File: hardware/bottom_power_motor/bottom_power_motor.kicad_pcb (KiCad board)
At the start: 2 copper layers, 52 x 52 mm, 104 parts, among them J1 Power/Motor 6p, J2 J_STK_A, J3 J_STK_B, Q1 P-FET 40V 30A, U1 L78L12, U2 TPS54360, U2_CB 100n, U2_CO 47u, U2_CZ 3n3, U2_D 60V 3A, U2_L 10u, U2_RC 10k, U2_RH 53k6, U2_RL 10k2, U2_RT_R 100k, U3 TLV62569, U4 TPS54360, U4_CB 100n, U4_CO 22u, U4_CZ 3n3, U4_D 60V 3A, U4_L 33u, U4_RC 10k, U4_RH 68k1, U4_RL 10k0, U4_RT_R 100k

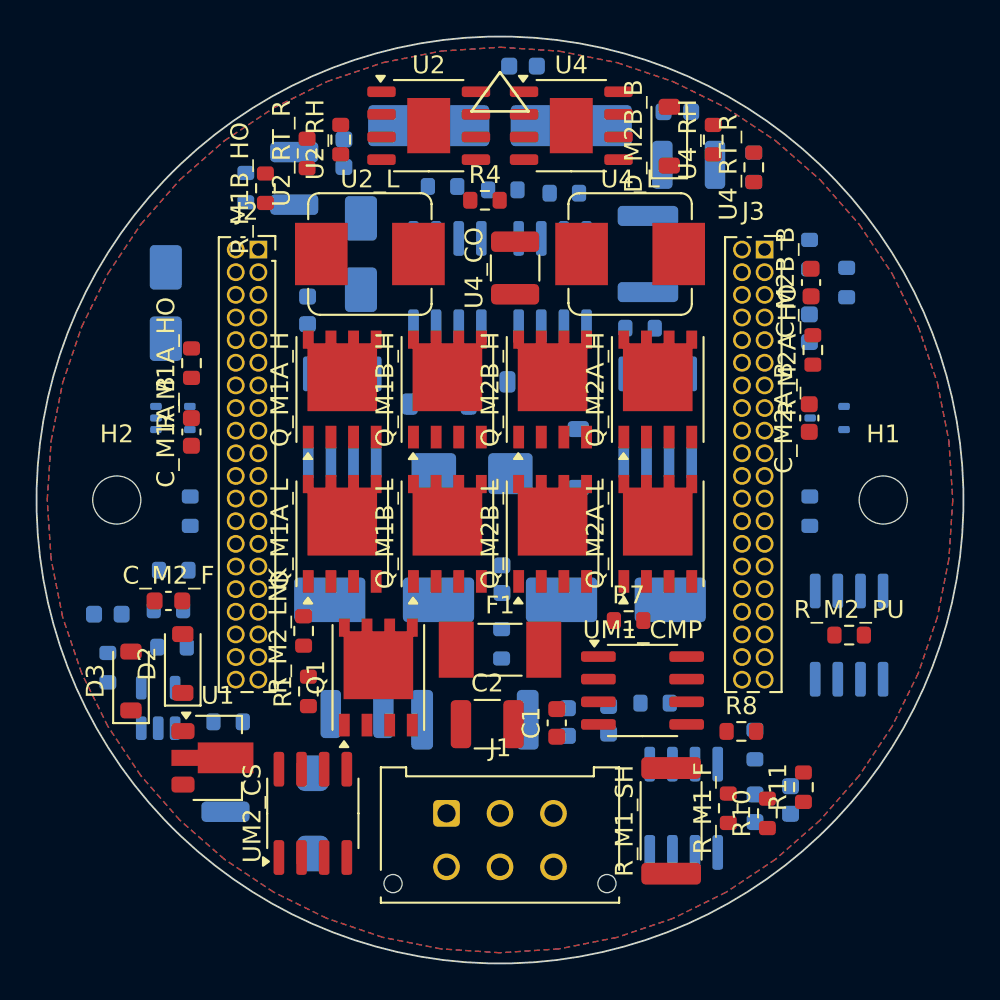
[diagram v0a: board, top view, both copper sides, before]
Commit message: Zwischenstand: Bottom neu geroutet, Top-Masse in Arbeit
Bottom: Neurouting mit 0,8-mm-Klasse - keine Kupferfehler mehr, aber
noch 62 offene Verbindungen; ein Fortsetzungslauf (Export mit
bestehender Verdrahtung, type route) konvergiert gerade weiter.
Top: Masse-Stichbahnen importiert und Zonen neu gefuellt (offene
PGND-Paare von 17 auf 7 reduziert); USB-Schirmpads A1/A12 per Stub an
die B-Reihe angebunden. Die restlichen 7 sitzen hinter USB-Datenbahnen
- USB_DP_C/DN_C, QSPI_D0 und RADAR_INT sind dafuer aufgerissen und
werden zusammen mit PGND als Netz neu verlegt (laeuft im Hintergrund).
route_boards: SWIG-Zaehlfehler nach SaveBoard umgangen (Zahlen kommen
aus dem eigenen SES-Import).

Co-Authored-By: Claude Fable 5 <noreply@anthropic.com>
Claude-Session: https://claude.ai/code/session_017FTFDJW9R41k2WFeDRNE3w
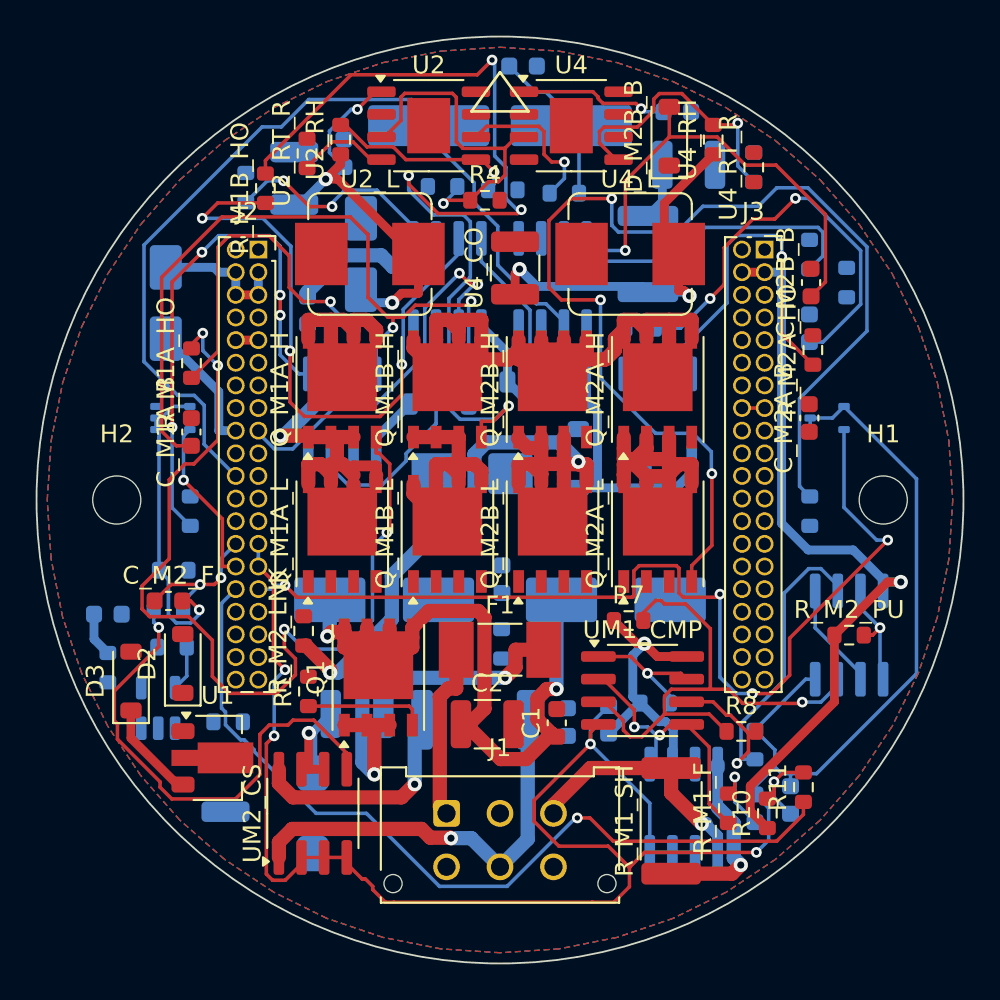
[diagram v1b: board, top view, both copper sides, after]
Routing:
- net AGND: track 0.00 -> 138.2 mm, vias 0 -> 5
- net 24V_PROT: track 0.00 -> 88.1 mm, vias 0 -> 2
- net 3V3_SYS: track 0.00 -> 68.5 mm, vias 0 -> 3
- net M2A_LO_GT: track 0.00 -> 65.2 mm, vias 0 -> 3
- net HW_TRIP2: track 0.00 -> 56.2 mm, vias 0 -> 4
- net M1B_HO_GT: track 0.00 -> 55.2 mm, vias 0 -> 4
- net M1A_HO_GT: track 0.00 -> 51.2 mm, vias 0 -> 4
- net M2_INB: track 0.00 -> 50.6 mm
- net TRIP_RST: track 0.00 -> 47.7 mm, vias 0 -> 1
- net M1A_VB: track 0.00 -> 43.6 mm, vias 0 -> 2
- net M2_SWB: track 0.00 -> 40.3 mm, vias 0 -> 2
- net M1B_HO_G: track 0.00 -> 35.5 mm, vias 0 -> 3
- net M2_ISNS: track 0.00 -> 33.7 mm, vias 0 -> 1
- net M1_SWA: track 0.00 -> 31.7 mm, vias 0 -> 2
- net M2_SWA: track 0.00 -> 30.1 mm, vias 0 -> 1
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
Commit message: Bottom: Standard-Vias und -Clearance fuer Leistungsklassen
Die 0,8er-Vias mit 0,2er-Clearance passen nicht in die Schluchten
zwischen den FET-Pads - die letzten ~50 Verbindungen blieben ueber
mehrere Stunden Autorouting dauerhaft offen. Jetzt 0,6/0,3-Vias und
0,15er-Clearance auch fuer PWR/RAIL auf dem Bottom-Board (2-3 A je
Via, ausreichend fuer Laufstrom und kurze Transienten; Handnacharbeit
der Leistungspfade vor Fertigung bleibt Pflicht per docs/05).
Bottom-Fortsetzungslauf mit den entspannten Regeln laeuft. Zudem
Bottom-Stand nach erster Fortsetzung (62 -> 53 offen) und Mid-Stand
nach finalem Wandnetz-Lauf (J3-25/33-Kette per Stich angebunden,
7 Paare offen, Iterator laeuft) uebernommen.

Co-Authored-By: Claude Fable 5 <noreply@anthropic.com>
Claude-Session: https://claude.ai/code/session_017FTFDJW9R41k2WFeDRNE3w
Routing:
- net U4_RT: track 0.00 -> 18.0 mm, vias 0 -> 2
- net AGND: track 138.2 -> 152.9 mm
- net 24V_GATE_P: track 6.79 -> 20.3 mm
- net 3V3_SYS: track 68.5 -> 80.7 mm, vias 3 -> 4
- net U4_SW: track 0.00 -> 9.59 mm, vias 0 -> 1
- net 5V_SYS: track 7.85 -> 16.9 mm
- net U3_FB: track 2.55 -> 6.21 mm, vias 0 -> 2
- net 24V_PROT: track 88.1 -> 90.4 mm

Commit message: Bottom: Fortsetzungsstand uebernommen (51 offen), frischer Lauf gestartet
Die Fortsetzung mit entspannten Regeln stagniert (53 -> 51 offen in
einer Stunde) - die unter den strikten Regeln entstandene Verdrahtung
verstopft die Korridore. Analog zum Mid-Board laeuft jetzt ein
frischer Komplettlauf mit den entspannten Klassen (0,8 mm-Bahnen,
0,6er-Vias, 0,15er-Clearance).

Co-Authored-By: Claude Fable 5 <noreply@anthropic.com>
Claude-Session: https://claude.ai/code/session_017FTFDJW9R41k2WFeDRNE3w
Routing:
- net U3_SW: track 0.00 -> 14.8 mm, vias 0 -> 2
- net 12V_RAW: track 8.04 -> 13.0 mm, vias 0 -> 1

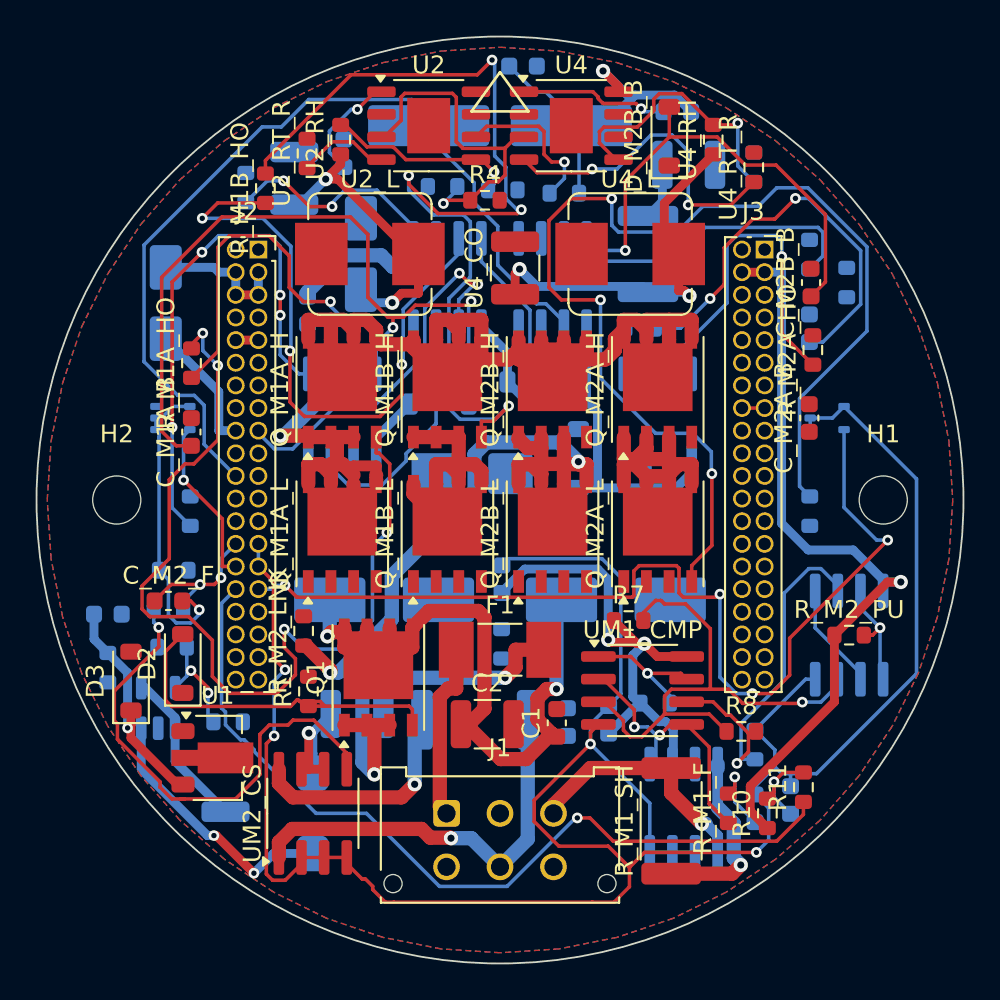
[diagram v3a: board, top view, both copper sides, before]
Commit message: Fertigungsdaten Top + Stuecklisten; Routing-Stand dokumentiert
hardware/fab/top_ui.zip (Gerber, Excellon inkl. PDF-Karte, Positionen)
nach bestandenem DRC-Gate; BOMs fuer alle drei Boards aus den
Schaltplan-Generatoren. README-Status und docs/05 um den ehrlichen
Routing-Stand ergaenzt: Top vollstaendig; Mid 10 PGND-Pour-Anbindungen
offen (Push-and-Shove-Handgriff); Bottom ~85 %, Leistungsteil ist
laut Pruefliste ohnehin Handarbeit. gnd_connect.py (Union-Find-
Clusteranalyse) als Werkzeug ergaenzt.

Co-Authored-By: Claude Fable 5 <noreply@anthropic.com>
Claude-Session: https://claude.ai/code/session_017FTFDJW9R41k2WFeDRNE3w
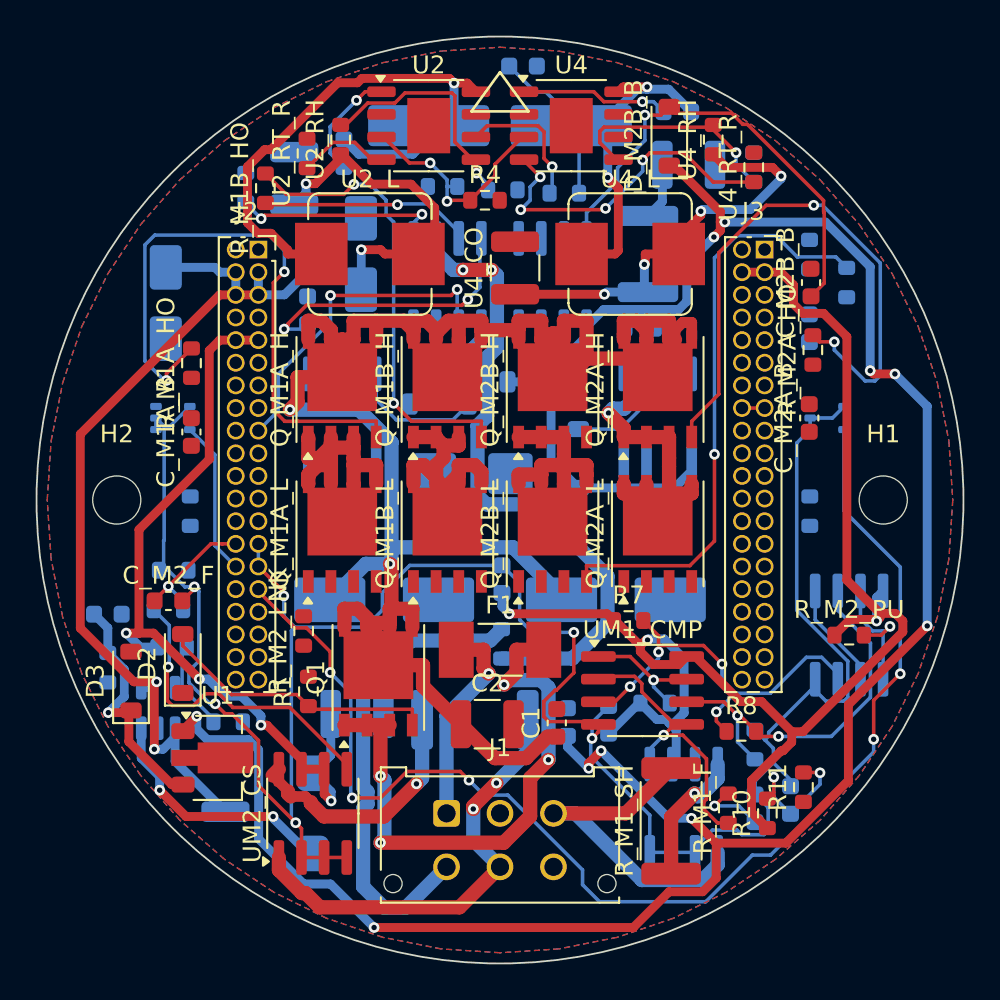
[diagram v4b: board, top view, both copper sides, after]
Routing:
- net 12V_GATE: track 29.2 -> 147.2 mm, vias 0 -> 10
- net M2A_LO_GT: track 65.2 -> 0.00 mm, vias 3 -> 0
- net M2_INB: track 50.6 -> 0.00 mm
- net TRIP_RST: track 47.7 -> 0.00 mm, vias 1 -> 0
- net 3V3_SYS: track 80.7 -> 127.8 mm, vias 4 -> 7
- net 5V_SYS: track 16.9 -> 56.1 mm, vias 0 -> 2
- net M1A_VB: track 43.6 -> 7.47 mm, vias 2 -> 0
- net M2A_HO_GT: track 0.00 -> 34.0 mm, vias 0 -> 2
- net U2_SW: track 0.00 -> 33.5 mm, vias 0 -> 1
- net M2B_LO_GT: track 0.00 -> 33.2 mm, vias 0 -> 1
- net M1A_LO_G: track 29.6 -> 0.00 mm, vias 4 -> 0
- net M1B_HO_GT: track 55.2 -> 25.7 mm, vias 4 -> 2
- net M1_SWB: track 24.5 -> 51.3 mm, vias 0 -> 2
- net M1_B: track 0.00 -> 26.6 mm
- net M2_SWB: track 40.3 -> 14.0 mm, vias 2 -> 0
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
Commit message: Bottom: bester Routing-Stand uebernommen (43 offen, 0 Kupferfehler)
Fortsetzungslauf auf der frischen Basis: 985 Segmente, 102 Vias,
43 offene Signalverbindungen im Motor-/Leistungsteil (vorher 47),
18 PGND/AGND-Pour-Anbindungen. Zonen wie beim Mid auf Vollanbindung
und 0,15er-Clearance umgestellt; keine harten DRC-Fehler mehr.
docs/05 mit den finalen Zahlen.

Co-Authored-By: Claude Fable 5 <noreply@anthropic.com>
Claude-Session: https://claude.ai/code/session_017FTFDJW9R41k2WFeDRNE3w
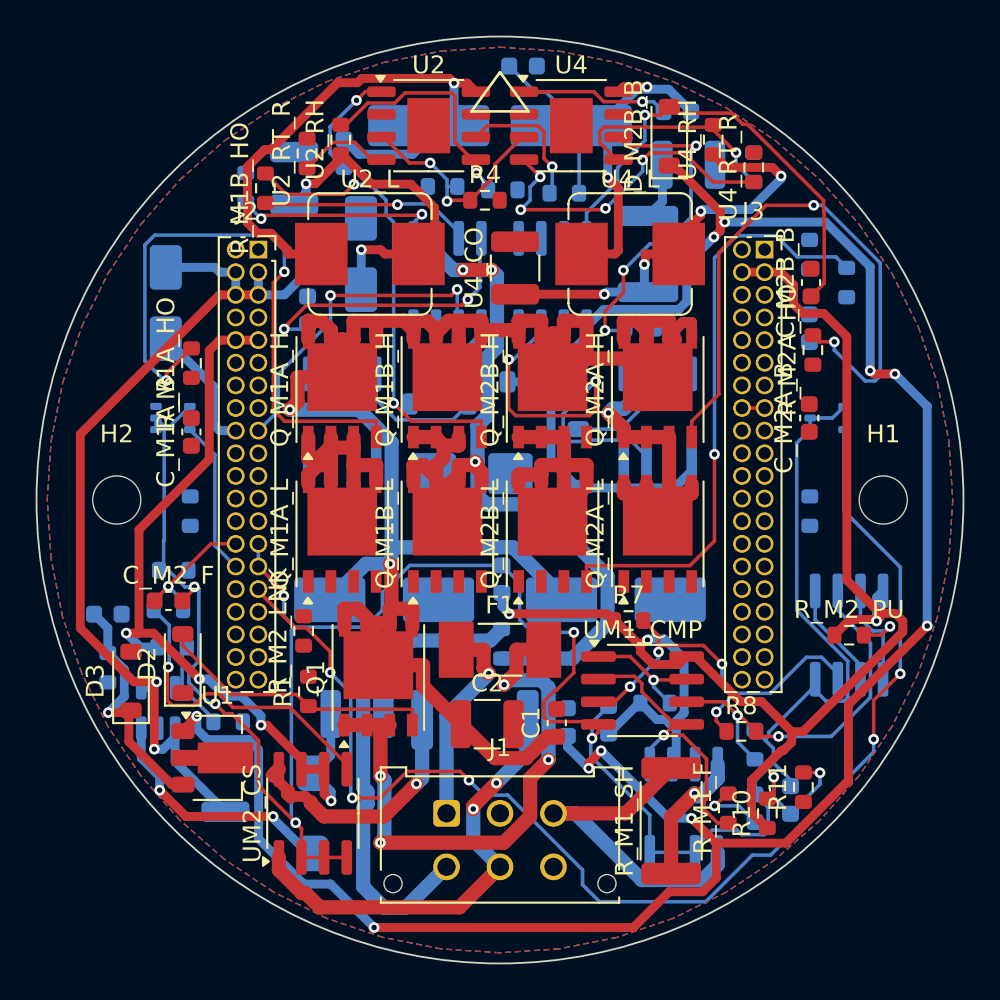
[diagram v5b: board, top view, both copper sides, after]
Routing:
- net M2_SD: track 0.00 -> 21.7 mm, vias 0 -> 2
- net U4_COMP: track 0.00 -> 18.7 mm, vias 0 -> 3
- net USB_VBUS: track 0.00 -> 7.31 mm
- net M1_SWB: track 51.3 -> 51.8 mm, vias 2 -> 3
